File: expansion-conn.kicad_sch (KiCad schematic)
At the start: 7 parts, among them J1 J_ERM8-040-05.0-L-DV-L-K-TR_S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

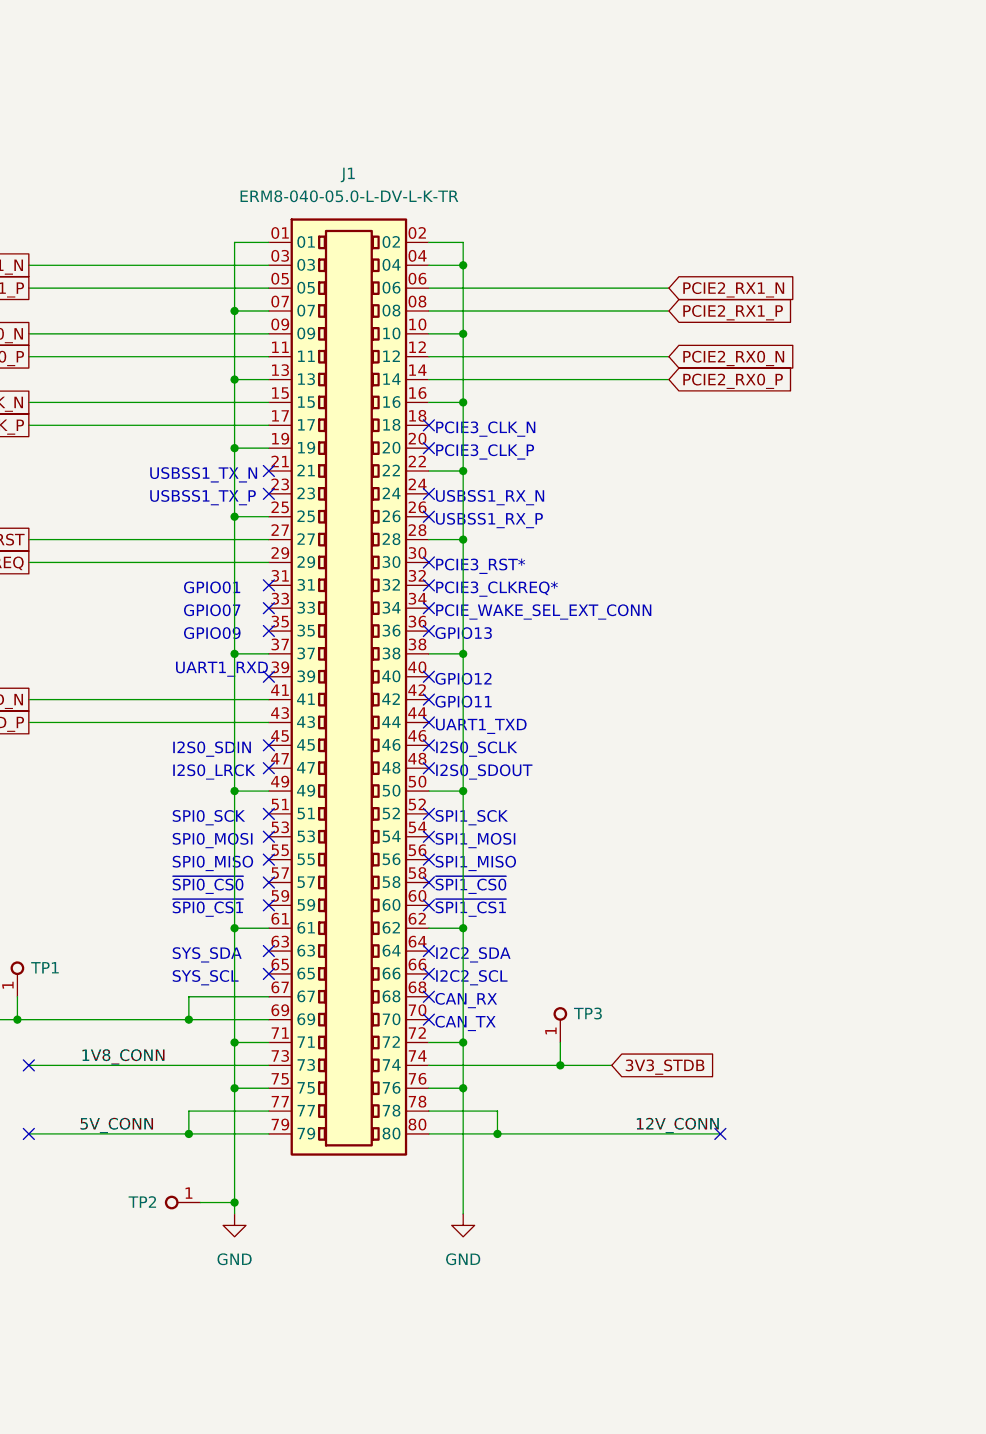
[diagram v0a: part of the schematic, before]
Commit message: Standardise samtech connector
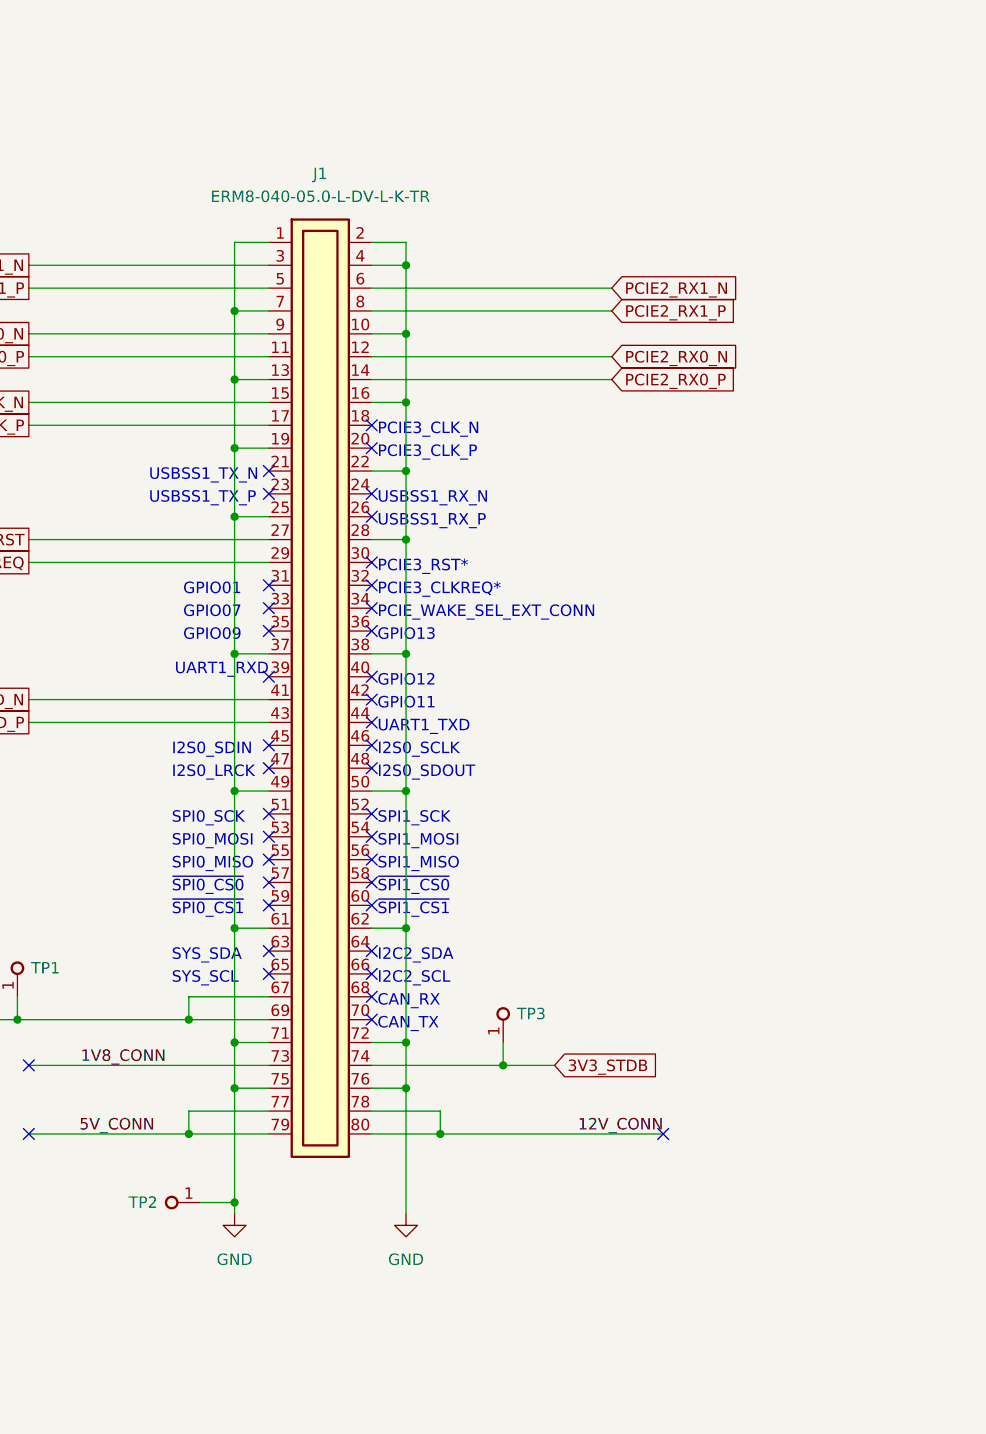
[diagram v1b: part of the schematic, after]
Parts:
- removed J1: J_ERM8-040-05.0-L-DV-L-K-TR_SAMTEC, antmicro-footprints:ERM8-040-05.0_SAMTEC, symbol antmicroB2bConnectors:J_ERM8-040-05.0-L-DV-L-K-TR_SAMTEC
- added J1: Plug_Samtec_ERM8_2x40_ERM8-040-05.0-L-DV-L-K-TR, antmicro-footprints:Conn_Plug_Samtec_ERM8_2x40_ERM8-040-05.0-L-DV-L-K-TR, symbol antmicroB2BConnectors:Plug_Samtec_ERM8_2x40_ERM8-040-05.0-L-DV-L-K-TR
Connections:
- net +3V3: now also J1.67, J1.69
- net 12V_CONN: now also J1.78, J1.80
- net 1V8_CONN: now also J1.73
- net 3V3_STDB: now also J1.74
- net 5V_CONN: now also J1.77, J1.79
- net GND: now also J1.1, J1.10, J1.13, J1.16, J1.19, J1.2, J1.22, J1.25, J1.28, J1.37, J1.38, J1.4, J1.49, J1.50, J1.61, J1.62, J1.7, J1.71, J1.72, J1.75, J1.76
- net PCIE2_CLKREQ: now also J1.29
- net PCIE2_CLK_N: now also J1.15
- net PCIE2_CLK_P: now also J1.17
- net PCIE2_RST: now also J1.27
- net PCIE2_RX0_N: now also J1.12
- net PCIE2_RX0_P: now also J1.14
- net PCIE2_RX1_N: now also J1.6
- net PCIE2_RX1_P: now also J1.8
- net PCIE2_TX0_N: now also J1.9
- net PCIE2_TX0_P: now also J1.11
- net PCIE2_TX1_N: now also J1.3
- net PCIE2_TX1_P: now also J1.5
- net USB1_D_N: now also J1.41
- net USB1_D_P: now also J1.43
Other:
- moved on the sheet: TP3

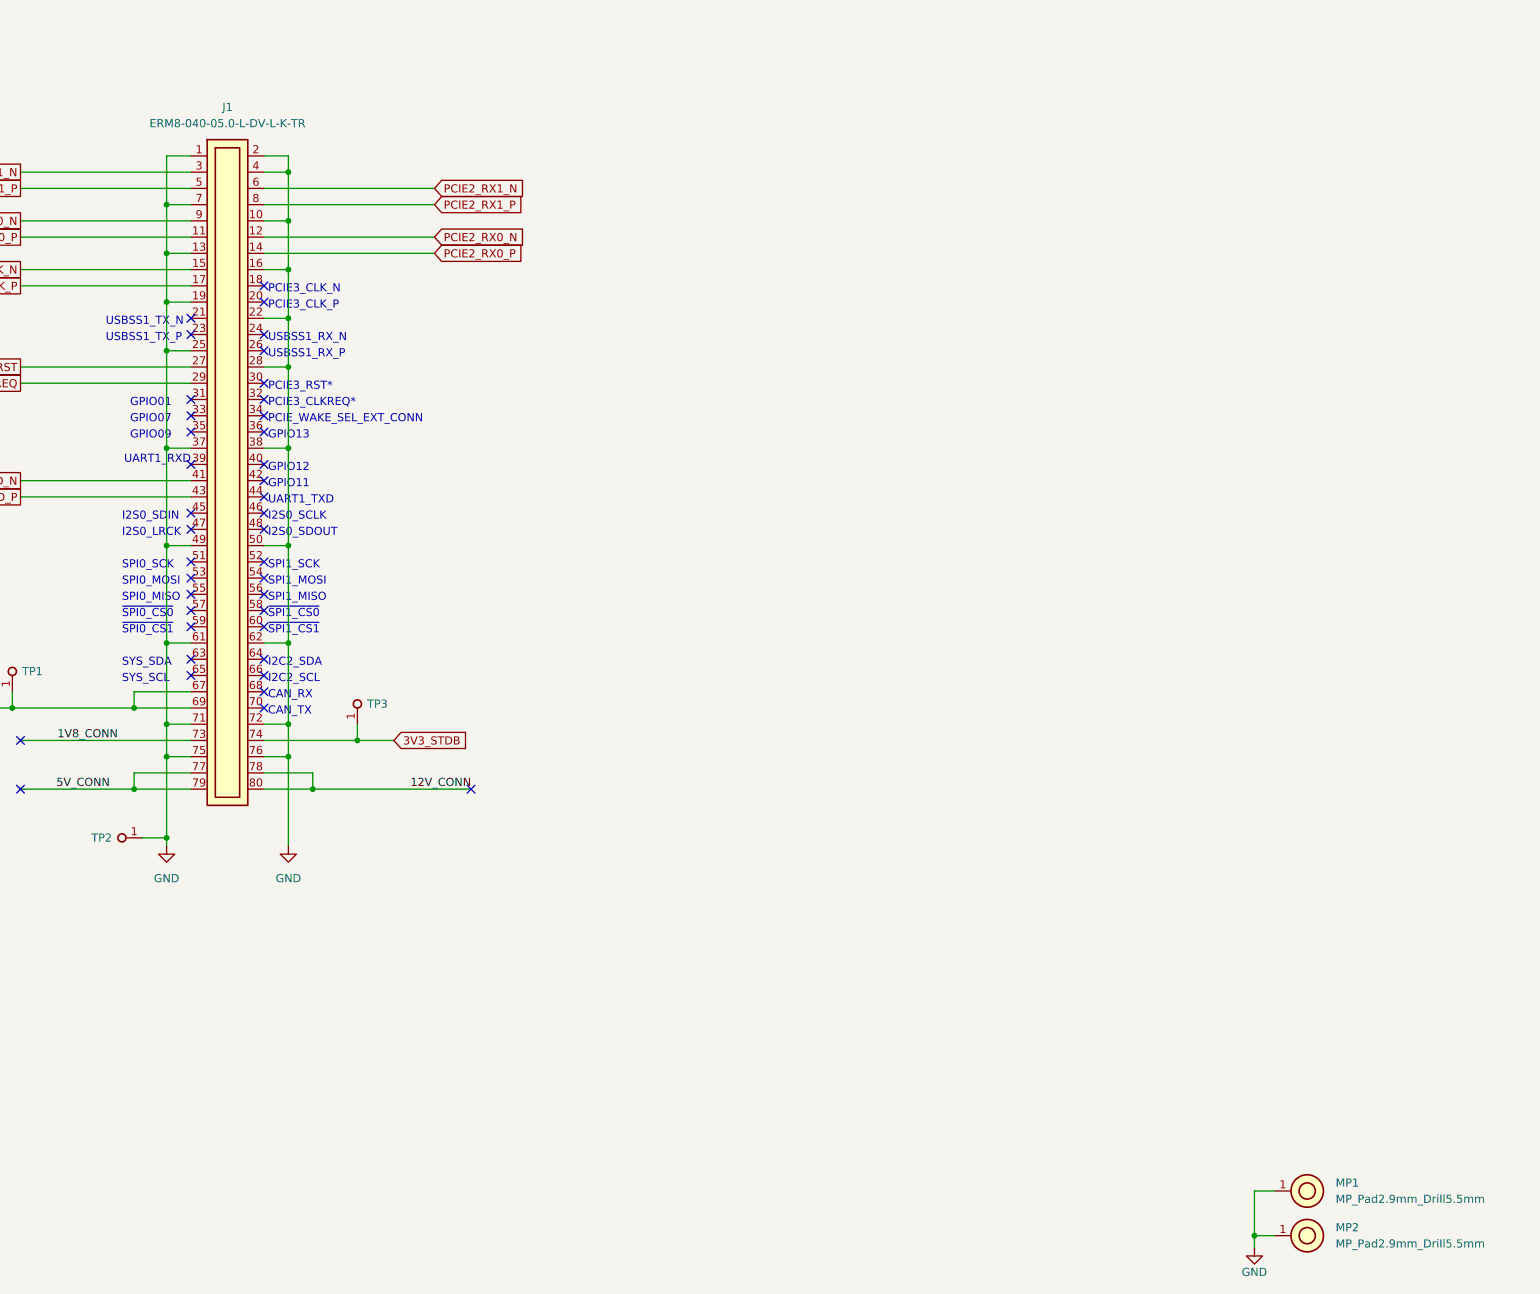
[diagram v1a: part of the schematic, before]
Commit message: [#56948] Update symbol/footprint links; Migrate to KiCad 7
[#56948] Update from lib; clean DRC

Remove Public False property from components
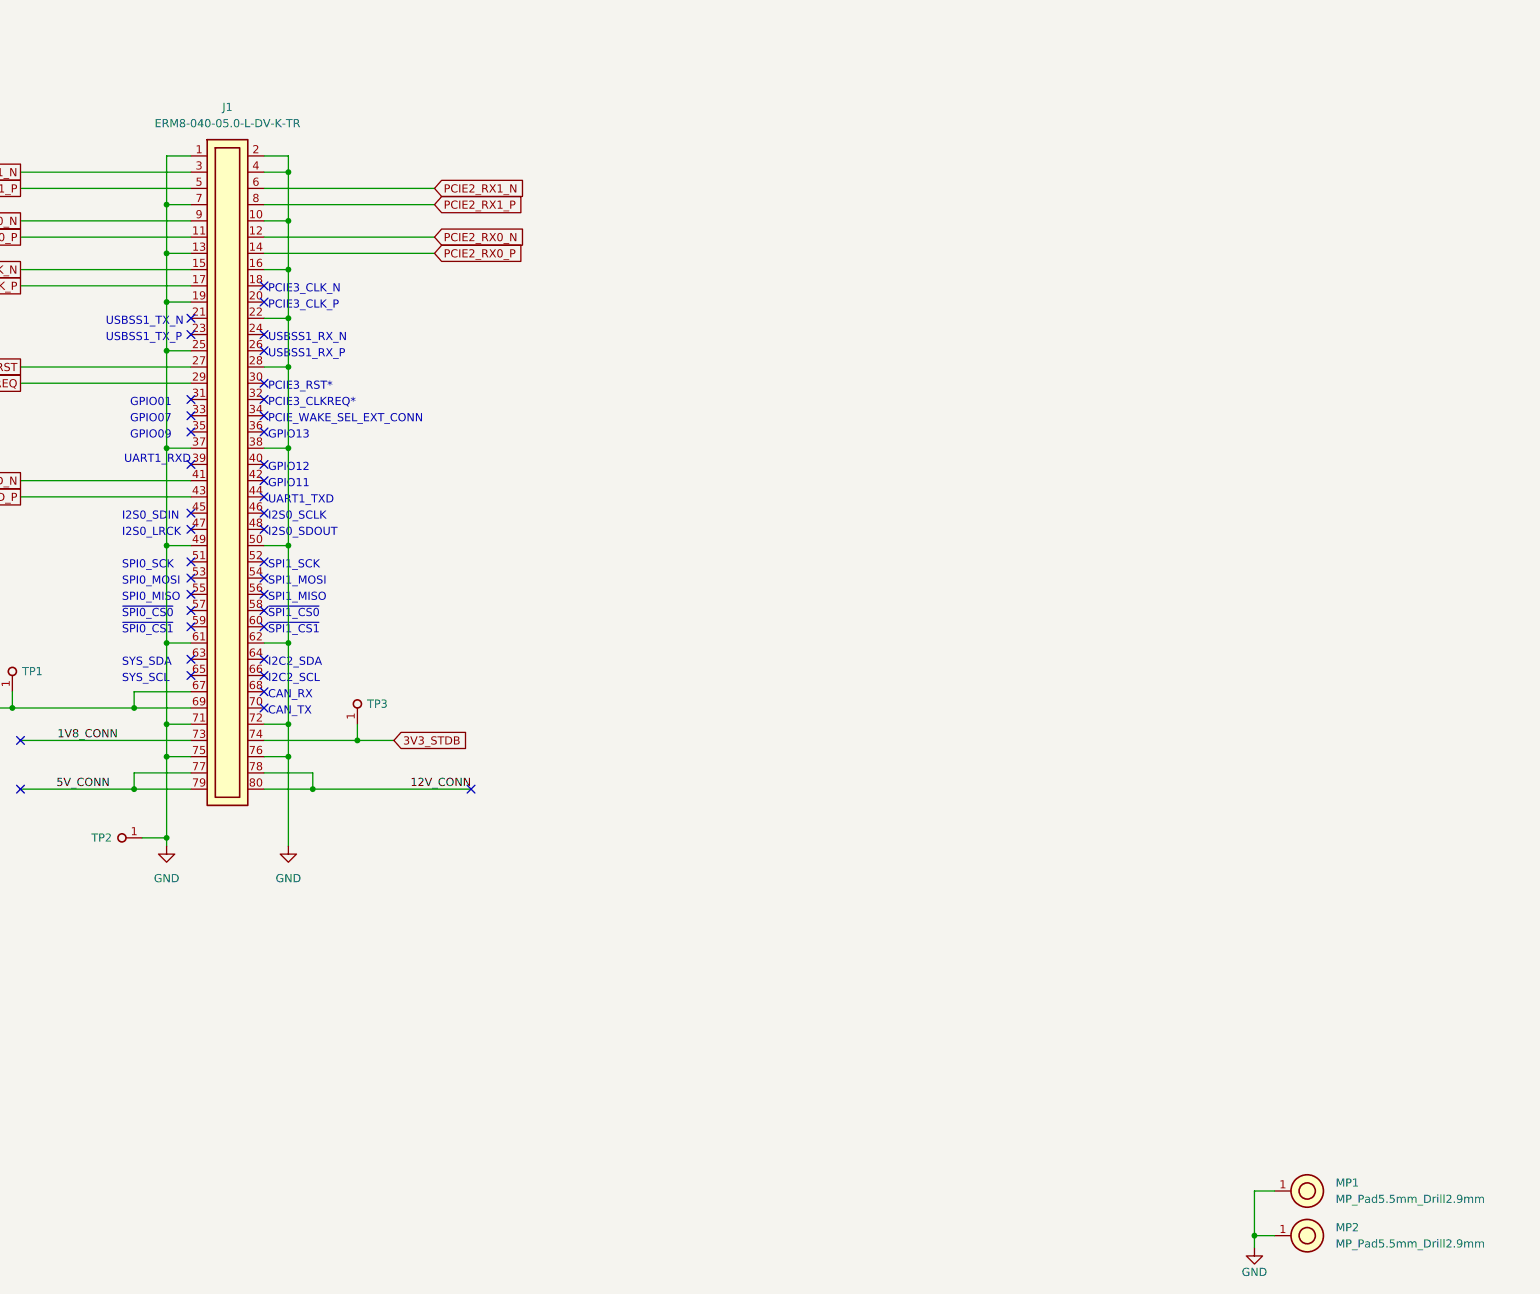
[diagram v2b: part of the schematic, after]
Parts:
- J1: value Plug_Samtec_ERM8_2x40_ERM8-040-05.0-L-DV-L-K-TR -> Plug_Samtec_ERM8_2x40_ERM8-040-05.0-L-DV-K-TR; footprint antmicro-footprints:Conn_Plug_Samtec_ERM8_2x40_ERM8-040-05.0-L-DV-L-K-TR -> antmicro-footprints:Conn_Plug_Samtec_ERM8_2x40_ERM8-040-05.0-L-DV-K-TR; symbol antmicroB2BConnectors:Plug_Samtec_ERM8_2x40_ERM8-040-05.0-L-DV-L-K-TR -> antmicroB2BConnectors:Plug_Samtec_ERM8_2x40_ERM8-040-05.0-L-DV-K-TR; MPN ERM8-040-05.0-L-DV-L-K-TR -> ERM8-040-05.0-L-DV-K-TR
- MP1, MP2: value MP_Pad2.9mm_Drill5.5mm -> MP_Pad5.5mm_Drill2.9mm; footprint antmicro-footprints:MP_Pad2.9mm_Drill5.5mm -> antmicro-footprints:MP_Pad5.5mm_Drill2.9mm; symbol antmicroMechanicalParts:MP_Pad2.9mm_Drill5.5mm -> antmicroMechanicalParts:MP_Pad5.5mm_Drill2.9mm; Public (none) -> False; now left out of the parts list
